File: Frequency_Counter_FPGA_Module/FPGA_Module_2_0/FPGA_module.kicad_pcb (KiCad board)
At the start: 4 copper layers, 98 x 89 mm, 281 parts, among them J1 Channel A, J10 REF_Test, J11 10MHz TTL, J12 10MHz TTL, J13 10MHz TTL, J14 10MHz TTL, J2 Channel B, J3 GPS, J4 Input_board, J5 STM_mainboard, J6 CLK_OUT_1, J7 CLK_OUT_2, J8 OCXO_OPA, J9 Ext. Ref., U1 MAX9601, U10 TMP117xxDRV, U11 TMP117xxDRV, U12 AD5693RxRM, U14 OPA365DBV, U15 OPA365DBV, U16 MIC920, U17 74LVC1G17, U18 MIC920, U19 TS5A3159DCK, U2 MC100EPT23DT, U20 74LVC1G17, U21 LMK1C1104, U22 LMK1C1104, U23 LMR33630ADDAR, U24 LMR33630ADDAR, U25 B0505S-1W, U3 MC100EP016A, U4 TLV9001IDCK, U5 MC100EPT23DT, U7 74LVC1G17, U8 ADS1115, U9 SI5356A

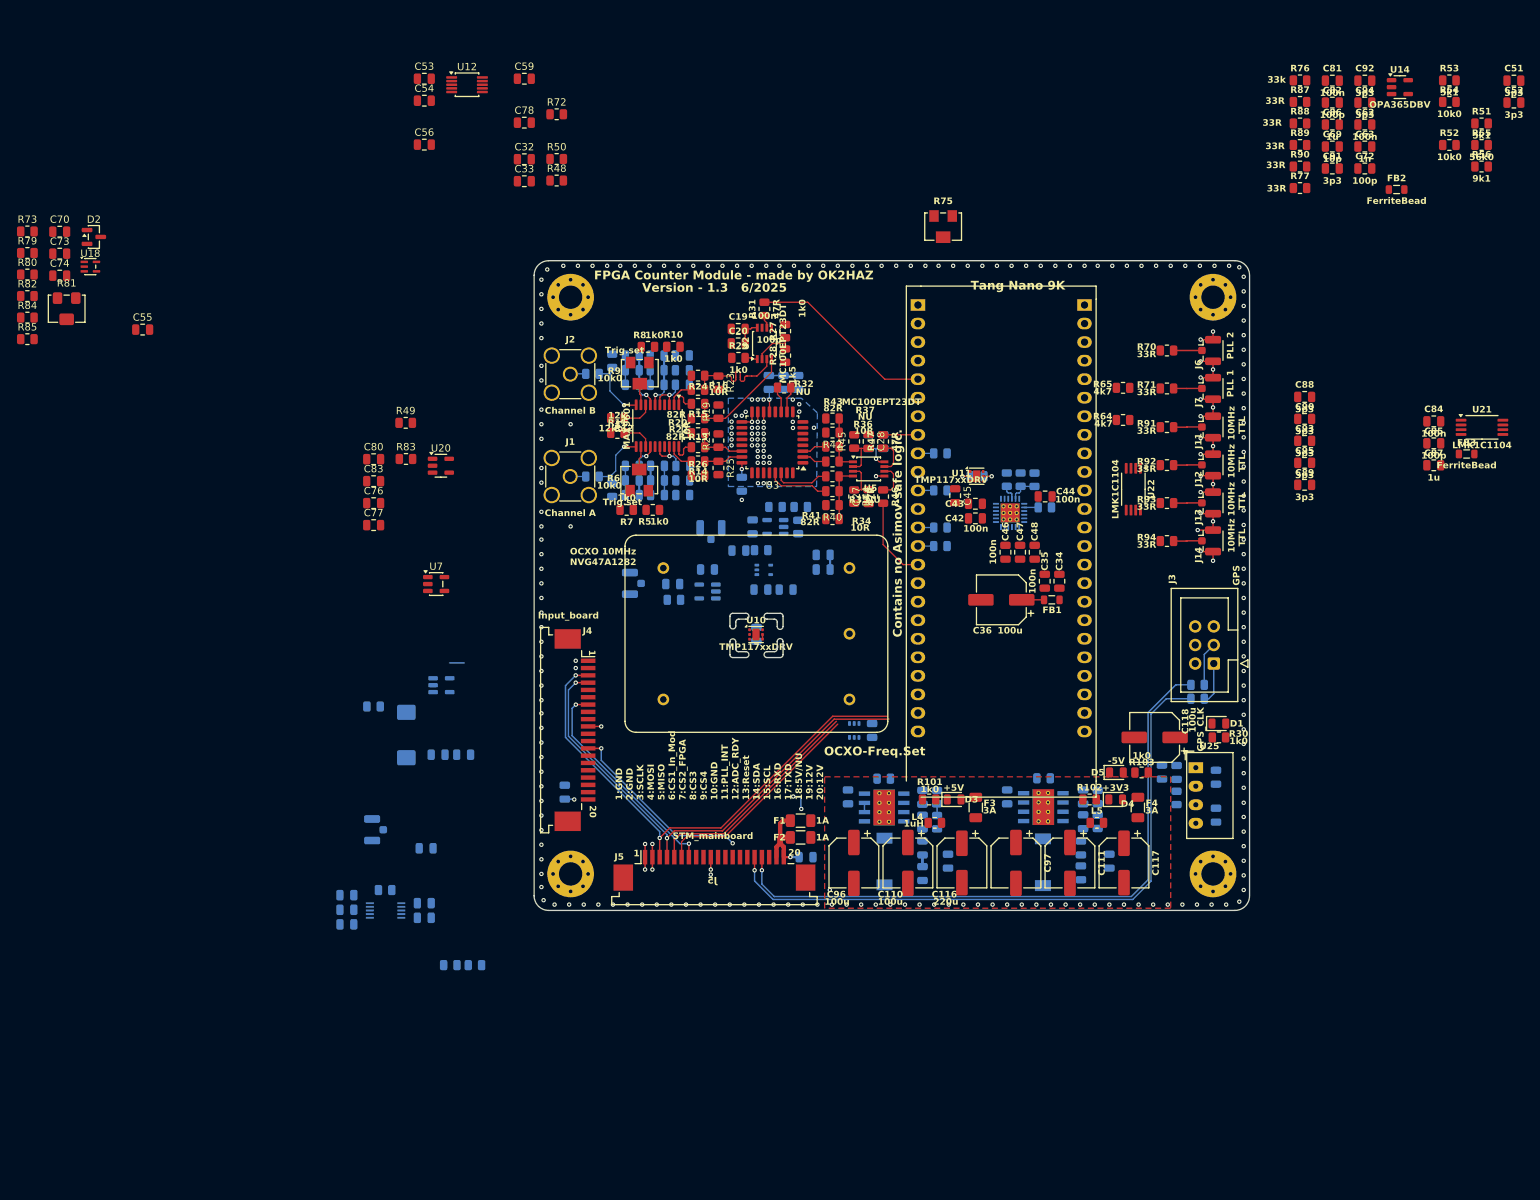
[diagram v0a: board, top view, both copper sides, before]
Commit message: feat(hw): FPGA carrier v2.0 — aktualizace schematu + PCB + checklist
KiCad FPGA_Module_2_0 (FPGA_Core/GPSDO/I2C_devices/power_supply schemata,
PCB layout, project), BOARD_V20_CHECKLIST.md. Odstranen zastaraly
FPGA_module_schematic.pdf (nahrazen exportem FPGA_module.pdf).

Co-Authored-By: OK2JNJ <ok2jnj@users.noreply.github.com>
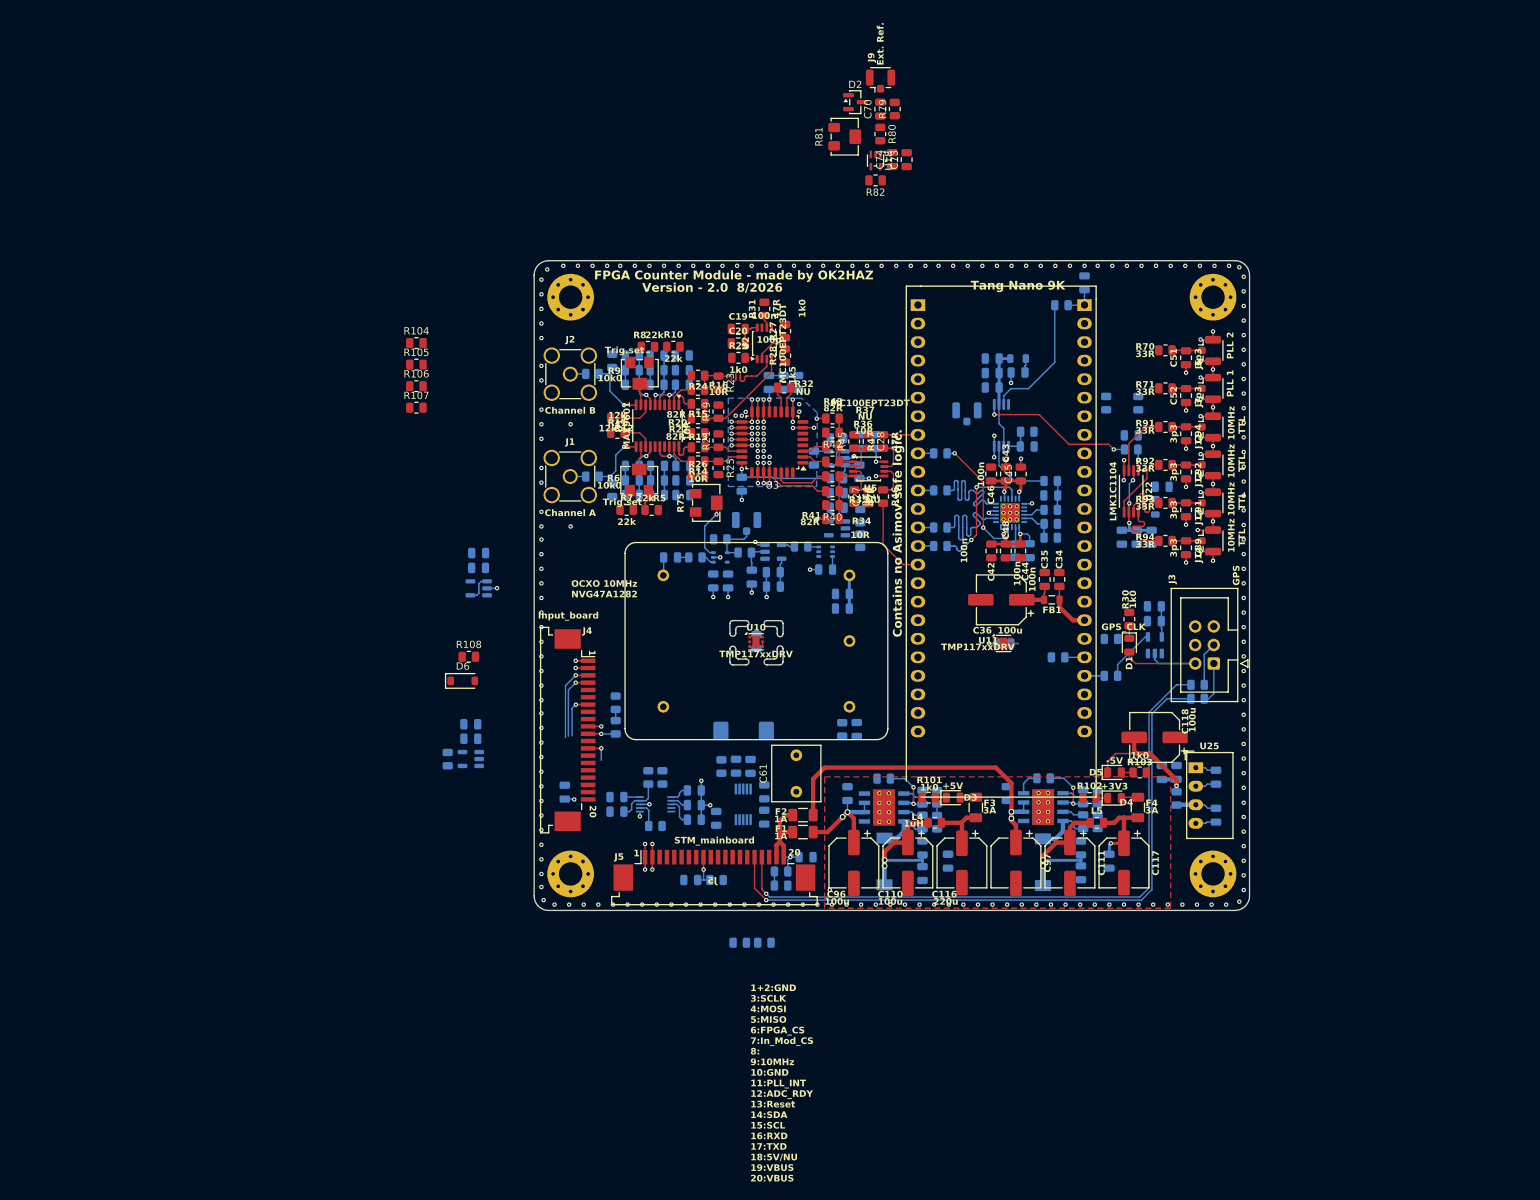
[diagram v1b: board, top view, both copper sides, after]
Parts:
- added D6: B0520LW, Diode_SMD:D_SOD-123, F.Cu at (40.2, 118.6)
- added R104: 12k, Resistor_SMD:R_0805_2012Metric, F.Cu at (33.9, 72.3)
- added R105: 12k, Resistor_SMD:R_0805_2012Metric, F.Cu at (33.9, 75.2)
- added R106: 12k, Resistor_SMD:R_0805_2012Metric, F.Cu at (33.9, 78.2)
- added R107: 12k, Resistor_SMD:R_0805_2012Metric, F.Cu at (33.9, 81.1)
- added R108: 100R, Resistor_SMD:R_0805_2012Metric, F.Cu at (41.1, 115.3)
- C32, C33, C47, C53, C54, C55, C56, C59, C62, C63, C69, C72, C76, C77, C78, C80, C81, C82, C83, C84, C85, C86, C87, C88, C90, C93, C95, FB2, FB3, R48, R49, R50, R52, R54, R64, R65, R72, R73, R76, R77, R83, R84, R85, R87, R88, R89, R90, U12, U14, U20, U21, U7: moved to B.Cu
- C61: footprint Capacitor_SMD:C_0805_2012Metric -> Capacitor_THT:C_Rect_L7.5mm_W6.5mm_P5.00mm; moved to F.Cu
- J9: moved to F.Cu
- R10, R5, R7, R8: value 1k0 -> 22k
- R51: value 5k1 -> 15k; moved to B.Cu
- R53: value 5k1 -> 1k0; moved to B.Cu
- R55: value 56k0 -> 100k; moved to B.Cu
- R56: value 9k1 -> 4k99; moved to B.Cu
- R57: value 8k2 -> 15k
- moved R53 144.5 mm to (61.2, 124.9), turned to -90 degrees
- moved U14 143.6 mm to (42.4, 105.9), turned to 180 degrees
- moved R51 143.6 mm to (67.6, 131.8), turned to 90 degrees
- moved R54 140.8 mm to (61.2, 121.6), turned to -90 degrees
- moved R52 139.8 mm to (65.6, 131.8), turned to -90 degrees
- moved R55 138.2 mm to (83.8, 144.7)
- moved R56 137.5 mm to (83.8, 146.6), turned to 180 degrees
- moved C62 134.8 mm to (42.4, 101.1)
- moved C63 134.4 mm to (42.4, 103.1)
- moved R90 126.3 mm to (75.0, 145.8), turned to 180 degrees
- moved J9 123.7 mm to (97.4, 36.4), turned to 90 degrees
- moved R79 120.4 mm to (99.4, 40.2), turned to 90 degrees
- moved R80 118.4 mm to (97.4, 43.7), turned to -90 degrees
- moved R85 117.4 mm to (94.7, 99.4), turned to 90 degrees
- moved R84 117.3 mm to (94.7, 96.0), turned to 90 degrees
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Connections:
- C88 pad 1: unconnected-(C88-Pad1) -> 10MHz_GPSDO_CLK4
- C96 pad 1: +12V -> /Power_supply/VBUS1_Fused
- C97 pad 1: +12V -> /Power_supply/VBUS2_Fused
- C98 pad 2: +12V -> /Power_supply/VBUS1_Fused
- C99 pad 2: +12V -> /Power_supply/VBUS2_Fused
- F1 pad 2: +12V -> /Power_supply/VBUS1_Fused
- F2 pad 2: +12V -> /Power_supply/VBUS2_Fused
- J5 pad 9: unconnected-(J5-Pin_9-Pad9) -> 10MHz_GPSDO_CLK4
- R55 pad 2: +12V -> VBUS
- R69 pad 1: Net-(U9-CLK_6) -> /FPGA_core/PLL_CLK4
- R69 pad 2: /FPGA_core/PLL_CLK4 -> Net-(U9-CLK_6)
- R76 pad 1: Net-(U16-+) -> +3V3
- R8 pad 2: +3V3 -> +5V
- R82 pad 1: Net-(U18-+) -> +3V3
- R90 pad 2: unconnected-(C88-Pad1) -> 10MHz_GPSDO_CLK4
- U23 pad 2: +12V -> /Power_supply/VBUS1_Fused
- U23 pad 3: +12V -> /Power_supply/VBUS1_Fused
- U24 pad 2: +12V -> /Power_supply/VBUS2_Fused
- U24 pad 3: +12V -> /Power_supply/VBUS2_Fused
- U4 pad 1: Net-(U4-+) -> Net-(U4--)
- U4 pad 3: Net-(U4--) -> Net-(U4-+)
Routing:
- net GND: track 78.0 -> 158.9 mm, vias 260 -> 286
- net SCK: track 70.7 -> 10.8 mm, vias 2 -> 1
- net MOSI: track 68.8 -> 9.45 mm, vias 2 -> 1
- net +3V3: track 29.9 -> 86.3 mm, vias 5 -> 9
- net /Power_supply/VBUS2_Fused: track 0.00 -> 45.9 mm, vias 0 -> 2
- net MISO: track 31.3 -> 0.00 mm
- net FPGA_CS2: track 30.2 -> 0.00 mm
- net CH_B: track 25.4 -> 0.00 mm
- net Input_Mod_CS1: track 30.1 -> 6.16 mm, vias 2 -> 1
- net Net-(U9-CLK_4): track 0.00 -> 21.3 mm
- net Net-(U9-CLK_2): track 0.00 -> 21.3 mm
- net Net-(U21-1Y1): track 0.00 -> 21.2 mm, vias 0 -> 2
- net Net-(C106-Pad1): track 0.00 -> 21.2 mm, vias 0 -> 2
- net Reset: track 26.1 -> 6.15 mm, vias 2 -> 1
- net -5V: track 11.7 -> 31.4 mm, vias 1 -> 2
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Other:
- outline, holes or cut-outs redrawn
- board text added: "1+2:GND 3:SCLK 4:MOSI 5:MISO 6:FPGA_CS 7:In_Mod_CS 8: 9:10MHz 10:GND 11:PLL_INT 12:ADC_RDY 13:Reset 14:SDA 15:SCL 16:RXD 17:TXD 18:5V/NU 19:VBUS 20:VBUS"
- board text added: "10MHz_GPSDO_CLK3"
- board text added: "CLK"
- board text added: "FPGA_CS2"
- board text added: "GPS_CLK_Buff"
- board text added: "GPS_Ext_Int"
- board text added: "MISO"
- board text added: "MOSI"
- board text added: "Version - 2.0 8/2026"
- board text removed: "10MHz_GPSDO_TTL"
- board text removed: "1:GND 2:GND 3:SCLK 4:MOSI 5:MISO 6:CS1_In_Mod 7:CS2_FPGA 8:CS3 9:CS4 10:GND 11:PLL_INT 12:ADC_RDY 13:Reset 14:SDA 15:SCL 16:RXD 17:TXD 18:5V/NU 19:12V 20:12V"
- board text removed: "DIV_Out"
- board text removed: "DIV_Res"
- board text removed: "GPS_Time_Stamp"
- board text removed: "OCXO-Freq.Set"
- board text removed: "PLL_CLK5"
- board text removed: "PLL_CLK6"
- board text removed: "PLL_CLK7"
- board text removed: "PLL_CLK8"
- board text removed: "STM_CLK"
- board text removed: "STM_CS2"
- board text removed: "STM_MISO"
- board text removed: "STM_MOSI"
- board text removed: "Version - 1.3 6/2025"
